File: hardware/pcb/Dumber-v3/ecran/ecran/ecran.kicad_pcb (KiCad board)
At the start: 2 copper layers, 31.1 x 24 mm, 14 parts, among them J1 TE 1-84981-0

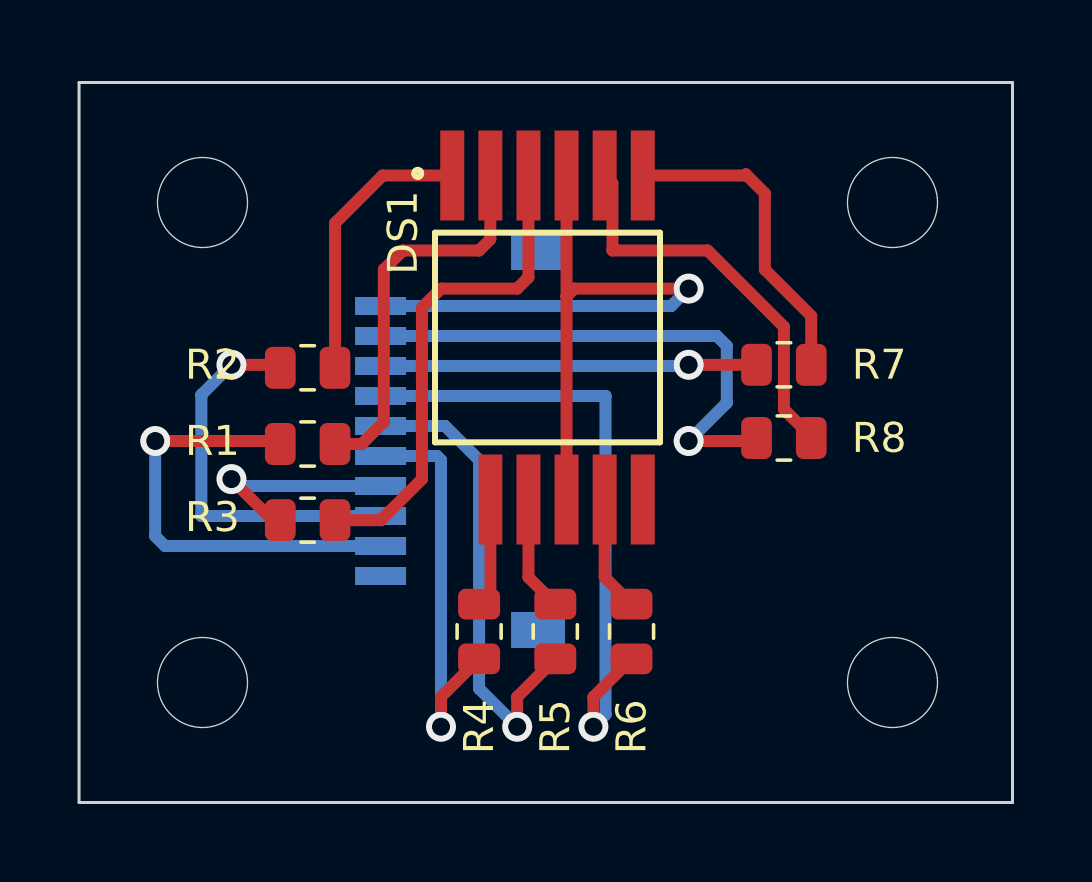
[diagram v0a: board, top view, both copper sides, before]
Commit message: asservissement moteur de base OK
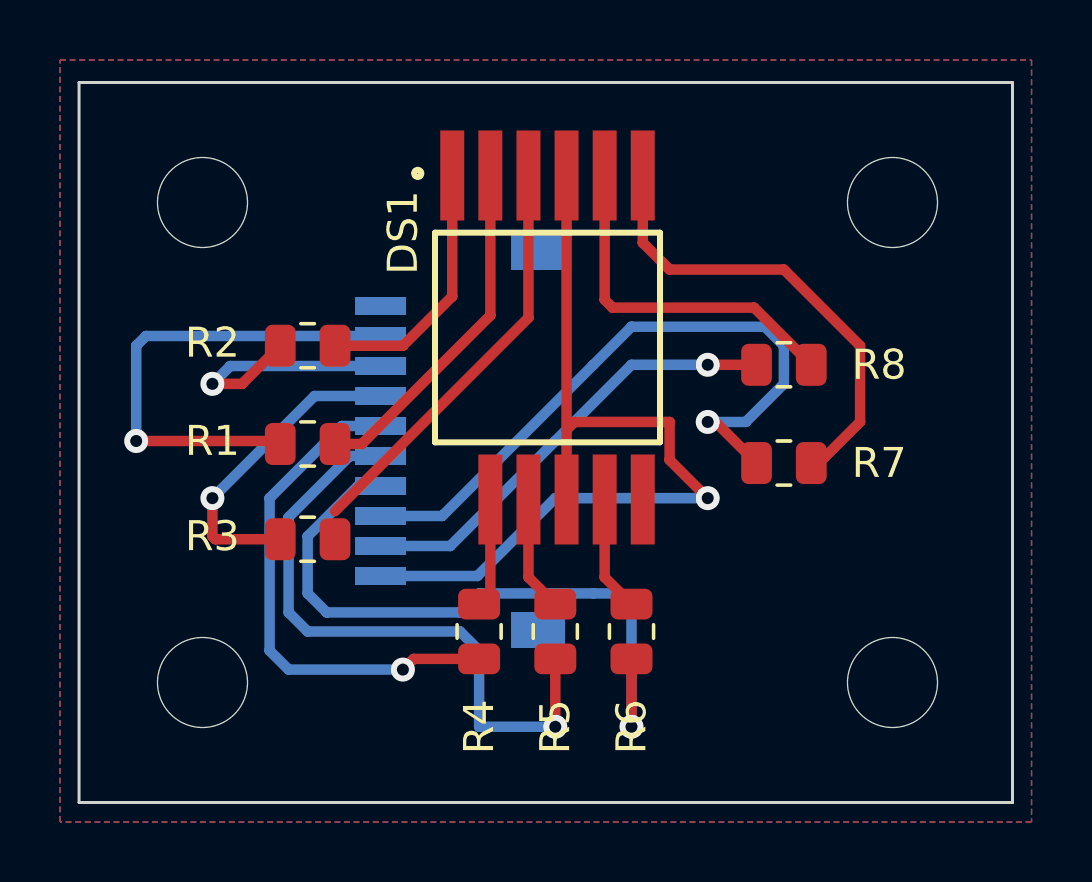
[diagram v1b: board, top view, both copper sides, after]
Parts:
- moved R7 3.28 mm to (119.4, 108.7)
- moved R8 2.44 mm to (119.4, 105.4)
- moved R2 0.73 mm to (103.5, 104.8)
- moved R3 0.63 mm to (103.5, 111.2)
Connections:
- J1 pad 1: GND -> unconnected-(J1-Pad1)
- J1 pad 10: unconnected-(J1-Pad10) -> GND
- J1 pad 2: Net-(J1-Pad2) -> Net-(R1-Pad1)
- J1 pad 3: Net-(J1-Pad3) -> Net-(R2-Pad1)
- J1 pad 4: Net-(J1-Pad4) -> Net-(R3-Pad1)
- J1 pad 5: Net-(J1-Pad5) -> Net-(R4-Pad1)
- J1 pad 6: Net-(J1-Pad6) -> Net-(R5-Pad1)
- J1 pad 7: Net-(J1-Pad7) -> Net-(R6-Pad1)
- J1 pad 8: Net-(J1-Pad8) -> Net-(R7-Pad1)
- J1 pad 9: Net-(J1-Pad9) -> Net-(R8-Pad1)
- R1 pad 1: Net-(J1-Pad9) -> Net-(R1-Pad1)
- R2 pad 1: Net-(J1-Pad8) -> Net-(R2-Pad1)
- R3 pad 1: Net-(J1-Pad7) -> Net-(R3-Pad1)
- R4 pad 1: Net-(J1-Pad6) -> Net-(R4-Pad1)
- R5 pad 1: Net-(J1-Pad5) -> Net-(R5-Pad1)
- R6 pad 1: Net-(J1-Pad4) -> Net-(R6-Pad1)
- R7 pad 1: Net-(J1-Pad3) -> Net-(R7-Pad1)
- R8 pad 1: Net-(J1-Pad2) -> Net-(R8-Pad1)
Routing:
- net Net-(R7-Pad1): track 0.00 -> 22.9 mm, vias 0 -> 1
- net Net-(R6-Pad1): track 0.00 -> 22.7 mm, vias 0 -> 1
- net Net-(J1-Pad4): track 21.5 -> 0.00 mm, vias 1 -> 0
- net Net-(R5-Pad1): track 0.00 -> 21.3 mm, vias 0 -> 1
- net Net-(J1-Pad2): track 17.7 -> 0.00 mm, vias 1 -> 0
- net Net-(R4-Pad1): track 0.00 -> 17.2 mm, vias 0 -> 1
- net Net-(R1-Pad1): track 0.00 -> 16.3 mm, vias 0 -> 1
- net Net-(J1-Pad5): track 16.0 -> 0.00 mm, vias 1 -> 0
- net Net-(R8-Pad1): track 0.00 -> 15.0 mm, vias 0 -> 1
- net Net-(J1-Pad9): track 15.0 -> 0.00 mm, vias 1 -> 0
- net Net-(J1-Pad6): track 13.7 -> 0.00 mm, vias 1 -> 0
- net Net-(J1-Pad8): track 13.1 -> 0.00 mm, vias 1 -> 0
- net Net-(J1-Pad3): track 12.5 -> 0.00 mm, vias 1 -> 0
- net Net-(R3-Pad1): track 0.00 -> 10.6 mm, vias 0 -> 1
- net Net-(R2-Pad1): track 0.00 -> 8.64 mm, vias 0 -> 1
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- added copper zone on B.Cu, net GND
- added copper zone on F.Cu, net GND

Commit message: remarche mais probleme probable de fragmentation memoire
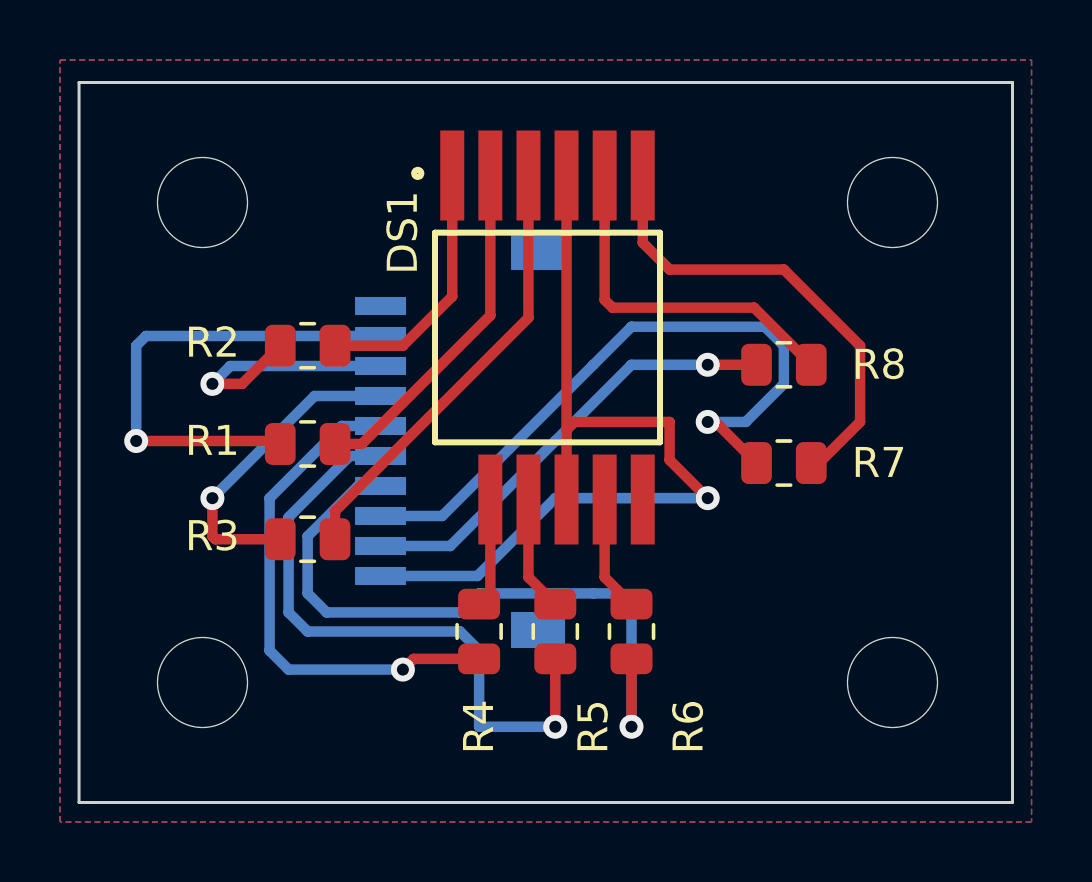
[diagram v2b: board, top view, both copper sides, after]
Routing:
- net Net-(DS1-Pad3): track 13.9 -> 14.8 mm
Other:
- board text added: "Ecran Dumber V1.1 04/23 - INSA GEI"
- board text removed: "Ecran Dumber V1.0 02/23 - INSA GEI"
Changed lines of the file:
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@@
   (title_block
     (title "Ecran pour Dumber")
-    (date "2023-02-17")
-    (rev "V1.0")
+    (date "2023-04-18")
+    (rev "V1.1")
     (company "INSA GEI")
   )
@@
   (net 10 "unconnected-(DS1-Pad7)")
   (net 11 "unconnected-(J1-Pad1)")
-  (net 12 "Net-(R1-Pad1)")
-  (net 13 "Net-(R2-Pad1)")
-  (net 14 "Net-(R3-Pad1)")
-  (net 15 "Net-(R4-Pad1)")
-  (net 16 "Net-(R5-Pad1)")
-  (net 17 "Net-(R6-Pad1)")
-  (net 18 "Net-(R7-Pad1)")
-  (net 19 "Net-(R8-Pad1)")
+  (net 12 "Net-(J1-Pad2)")
+  (net 13 "Net-(J1-Pad3)")
+  (net 14 "Net-(J1-Pad4)")
+  (net 15 "Net-(J1-Pad5)")
+  (net 16 "Net-(J1-Pad6)")
+  (net 17 "Net-(J1-Pad7)")
+  (net 18 "Net-(J1-Pad8)")
+  (net 19 "Net-(J1-Pad9)")
   (footprint "Resistor_SMD:R_0805_2012Metric" (layer "F.Cu")
     (at 111.76 114.3 90)
@@
     (property "Sheetname" "")
     (attr smd)
-    (fp_text reference "R5" (at -3.175 0 90) (layer "F.SilkS")
+    (fp_text reference "R5" (at -3.175 1.27 90) (layer "F.SilkS")
       (effects (font (size 1 1) (thickness 0.15)))
     )
@@
     (fp_line (start 1 -0.625) (end 1 0.625) (layer "F.Fab") (width 0.1))
     (pad "1" smd roundrect (at -0.9125 0 90) (size 1.025 1.4) (layers "F.Cu" "F.Paste" "F.Mask") (roundrect_rratio 0.243902439)
-      (net 16 "Net-(R5-Pad1)") (pintype "passive"))
+      (net 16 "Net-(J1-Pad6)") (pintype "passive"))
     (pad "2" smd roundrect (at 0.9125 0 90) (size 1.025 1.4) (layers "F.Cu" "F.Paste" "F.Mask") (roundrect_rratio 0.243902439)
       (net 8 "Net-(DS1-Pad10)") (pintype "passive"))
@@
     (fp_line (start -1 -0.625) (end 1 -0.625) (layer "F.Fab") (width 0.1))
     (pad "1" smd roundrect (at -0.9125 0 90) (size 1.025 1.4) (layers "F.Cu" "F.Paste" "F.Mask") (roundrect_rratio 0.243902439)
-      (net 15 "Net-(R4-Pad1)") (pintype "passive"))
+      (net 15 "Net-(J1-Pad5)") (pintype "passive"))
     (pad "2" smd roundrect (at 0.9125 0 90) (size 1.025 1.4) (layers "F.Cu" "F.Paste" "F.Mask") (roundrect_rratio 0.243902439)
       (net 9 "Net-(DS1-Pad11)") (pintype "passive"))
@@
     (fp_line (start -1 -0.625) (end 1 -0.625) (layer "F.Fab") (width 0.1))
     (pad "1" smd roundrect (at -0.9125 0) (size 1.025 1.4) (layers "F.Cu" "F.Paste" "F.Mask") (roundrect_rratio 0.243902439)
-      (net 18 "Net-(R7-Pad1)") (pintype "passive"))
+      (net 18 "Net-(J1-Pad8)") (pintype "passive"))
     (pad "2" smd roundrect (at 0.9125 0) (size 1.025 1.4) (layers "F.Cu" "F.Paste" "F.Mask") (roundrect_rratio 0.243902439)
       (net 6 "Net-(DS1-Pad6)") (pintype "passive"))
@@
     (fp_line (start -1 0.625) (end -1 -0.625) (layer "F.Fab") (width 0.1))
     (pad "1" smd roundrect (at -0.9125 0) (size 1.025 1.4) (layers "F.Cu" "F.Paste" "F.Mask") (roundrect_rratio 0.243902439)
-      (net 13 "Net-(R2-Pad1)") (pintype "passive"))
+      (net 13 "Net-(J1-Pad3)") (pintype "passive"))
     (pad "2" smd roundrect (at 0.9125 0) (size 1.025 1.4) (layers "F.Cu" "F.Paste" "F.Mask") (roundrect_rratio 0.243902439)
       (net 1 "Net-(DS1-Pad1)") (pintype "passive"))
@@
     (fp_line (start -1 -0.625) (end 1 -0.625) (layer "F.Fab") (width 0.1))
     (pad "1" smd roundrect (at -0.9125 0) (size 1.025 1.4) (layers "F.Cu" "F.Paste" "F.Mask") (roundrect_rratio 0.243902439)
-      (net 19 "Net-(R8-Pad1)") (pintype "passive"))
+      (net 19 "Net-(J1-Pad9)") (pintype "passive"))
     (pad "2" smd roundrect (at 0.9125 0) (size 1.025 1.4) (layers "F.Cu" "F.Paste" "F.Mask") (roundrect_rratio 0.243902439)
       (net 5 "Net-(DS1-Pad5)") (pintype "passive"))
@@
     (property "Sheetname" "")
     (attr smd)
-    (fp_text reference "R6" (at -3.175 0 90) (layer "F.SilkS")
+    (fp_text reference "R6" (at -3.175 1.905 90) (layer "F.SilkS")
       (effects (font (size 1 1) (thickness 0.15)))
     )
@@
     (fp_line (start 1 -0.625) (end 1 0.625) (layer "F.Fab") (width 0.1))
     (pad "1" smd roundrect (at -0.9125 0 90) (size 1.025 1.4) (layers "F.Cu" "F.Paste" "F.Mask") (roundrect_rratio 0.243902439)
-      (net 17 "Net-(R6-Pad1)") (pintype "passive"))
+      (net 17 "Net-(J1-Pad7)") (pintype "passive"))
     (pad "2" smd roundrect (at 0.9125 0 90) (size 1.025 1.4) (layers "F.Cu" "F.Paste" "F.Mask") (roundrect_rratio 0.243902439)
       (net 7 "Net-(DS1-Pad8)") (pintype "passive"))
@@
     (fp_line (start 1 -0.625) (end 1 0.625) (layer "F.Fab") (width 0.1))
     (pad "1" smd roundrect (at -0.9125 0) (size 1.025 1.4) (layers "F.Cu" "F.Paste" "F.Mask") (roundrect_rratio 0.243902439)
-      (net 14 "Net-(R3-Pad1)") (pintype "passive"))
+      (net 14 "Net-(J1-Pad4)") (pintype "passive"))
     (pad "2" smd roundrect (at 0.9125 0) (size 1.025 1.4) (layers "F.Cu" "F.Paste" "F.Mask") (roundrect_rratio 0.243902439)
       (net 4 "Net-(DS1-Pad3)") (pintype "passive"))
@@
     (fp_line (start 1 0.625) (end -1 0.625) (layer "F.Fab") (width 0.1))
     (pad "1" smd roundrect (at -0.9125 0) (size 1.025 1.4) (layers "F.Cu" "F.Paste" "F.Mask") (roundrect_rratio 0.243902439)
-      (net 12 "Net-(R1-Pad1)") (pintype "passive"))
+      (net 12 "Net-(J1-Pad2)") (pintype "passive"))
     (pad "2" smd roundrect (at 0.9125 0) (size 1.025 1.4) (layers "F.Cu" "F.Paste" "F.Mask") (roundrect_rratio 0.243902439)
       (net 2 "Net-(DS1-Pad2)") (pintype "passive"))
@@
       (net 11 "unconnected-(J1-Pad1)") (pinfunction "Pin_1") (pintype "passive+no_connect"))
     (pad "2" smd rect locked (at -3.5 0.35 270) (size 0.6 1.7) (layers "B.Cu" "B.Paste" "B.Mask")
-      (net 12 "Net-(R1-Pad1)") (pinfunction "Pin_2") (pintype "passive"))
+      (net 12 "Net-(J1-Pad2)") (pinfunction "Pin_2") (pintype "passive"))
     (pad "3" smd rect locked (at -2.5 0.35 270) (size 0.6 1.7) (layers "B.Cu" "B.Paste" "B.Mask")
-      (net 13 "Net-(R2-Pad1)") (pinfunction "Pin_3") (pintype "passive"))
+      (net 13 "Net-(J1-Pad3)") (pinfunction "Pin_3") (pintype "passive"))
     (pad "4" smd rect locked (at -1.5 0.35 270) (size 0.6 1.7) (layers "B.Cu" "B.Paste" "B.Mask")
-      (net 14 "Net-(R3-Pad1)") (pinfunction "Pin_4") (pintype "passive"))
+      (net 14 "Net-(J1-Pad4)") (pinfunction "Pin_4") (pintype "passive"))
     (pad "5" smd rect locked (at -0.5 0.35 270) (size 0.6 1.7) (layers "B.Cu" "B.Paste" "B.Mask")
-      (net 15 "Net-(R4-Pad1)") (pinfunction "Pin_5") (pintype "passive"))
+      (net 15 "Net-(J1-Pad5)") (pinfunction "Pin_5") (pintype "passive"))
     (pad "6" smd rect locked (at 0.5 0.35 270) (size 0.6 1.7) (layers "B.Cu" "B.Paste" "B.Mask")
-      (net 16 "Net-(R5-Pad1)") (pinfunction "Pin_6") (pintype "passive"))
+      (net 16 "Net-(J1-Pad6)") (pinfunction "Pin_6") (pintype "passive"))
     (pad "7" smd rect locked (at 1.5 0.35 270) (size 0.6 1.7) (layers "B.Cu" "B.Paste" "B.Mask")
-      (net 17 "Net-(R6-Pad1)") (pinfunction "Pin_7") (pintype "passive"))
+      (net 17 "Net-(J1-Pad7)") (pinfunction "Pin_7") (pintype "passive"))
     (pad "8" smd rect locked (at 2.5 0.35 270) (size 0.6 1.7) (layers "B.Cu" "B.Paste" "B.Mask")
-      (net 18 "Net-(R7-Pad1)") (pinfunction "Pin_8") (pintype "passive"))
+      (net 18 "Net-(J1-Pad8)") (pinfunction "Pin_8") (pintype "passive"))
     (pad "9" smd rect locked (at 3.5 0.35 270) (size 0.6 1.7) (layers "B.Cu" "B.Paste" "B.Mask")
-      (net 19 "Net-(R8-Pad1)") (pinfunction "Pin_9") (pintype "passive"))
+      (net 19 "Net-(J1-Pad9)") (pinfunction "Pin_9") (pintype "passive"))
     (pad "10" smd rect locked (at 4.5 0.35 270) (size 0.6 1.7) (layers "B.Cu" "B.Paste" "B.Mask")
       (net 3 "GND") (pinfunction "Pin_10") (pintype "passive"))
@@
   (gr_line (start 95.885 120) (end 95.885 96) (layer "Edge.Cuts") (width 0.1))
   (gr_line (start 95.885 96) (end 127 96) (layer "Edge.Cuts") (width 0.1))
-  (gr_text "Ecran Dumber\nV1.0\n02/23 - INSA GEI" (at 116.205 107.95 270) (layer "B.SilkS")
+  (gr_text "Ecran Dumber\nV1.1\n04/23 - INSA GEI" (at 116.205 107.95 270) (layer "B.SilkS")
     (effects (font (size 1 1) (thickness 0.15)) (justify mirror))
   )
@@
   (segment (start 110.865 103.8425) (end 104.4175 110.29) (width 0.35) (layer "F.Cu") (net 4))
   (segment (start 110.865 99.1) (end 110.865 103.8425) (width 0.35) (layer "F.Cu") (net 4))
+  (segment (start 104.4175 110.29) (end 104.4175 111.225) (width 0.35) (layer "F.Cu") (net 4))
   (segment (start 118.3875 103.505) (end 113.665 103.505) (width 0.35) (layer "F.Cu") (net 5))
   (segment (start 113.665 103.505) (end 113.405 103.245) (width 0.35) (layer "F.Cu") (net 5))
